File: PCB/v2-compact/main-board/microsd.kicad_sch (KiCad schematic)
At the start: 0 parts

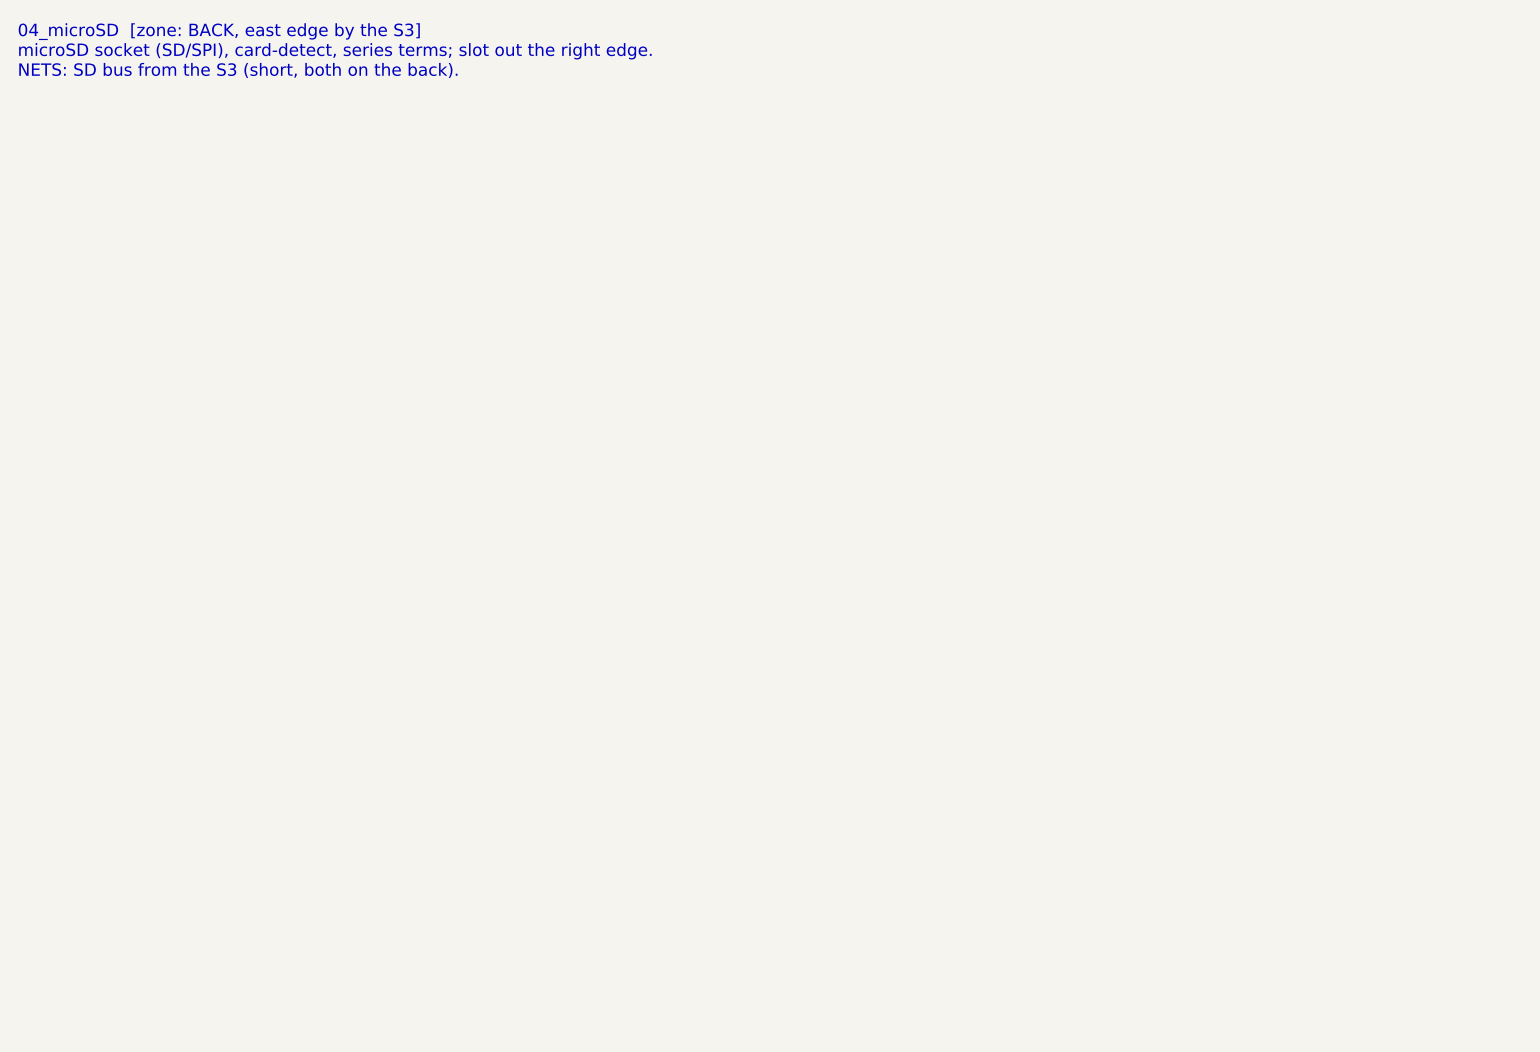
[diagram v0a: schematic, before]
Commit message: Schematics: main board ESP32-S3, microSD, and display/UI sheets
- 02_ESP32-S3: the brain. Shared SPI (LCD_SCK/MOSI + SD_MISO) for TFT and
  microSD, USB data to the USB-C through the ESD, and the full J1 interface to
  the shield (C5 UART + DRDY, I2C to PN532, RV1106 UART, IR, 1-Wire). EN/boot RC
  + decoupling.
- 04_microSD: SPI-mode card with CS pull-up + decoupling.
- 03_Display_UI: SPI TFT header, five nav buttons to GND, two status LEDs.

Netlist-verified: the S3 ties in the other end of every J1 net (isolated labels
on the main board dropped from 12 to 1).
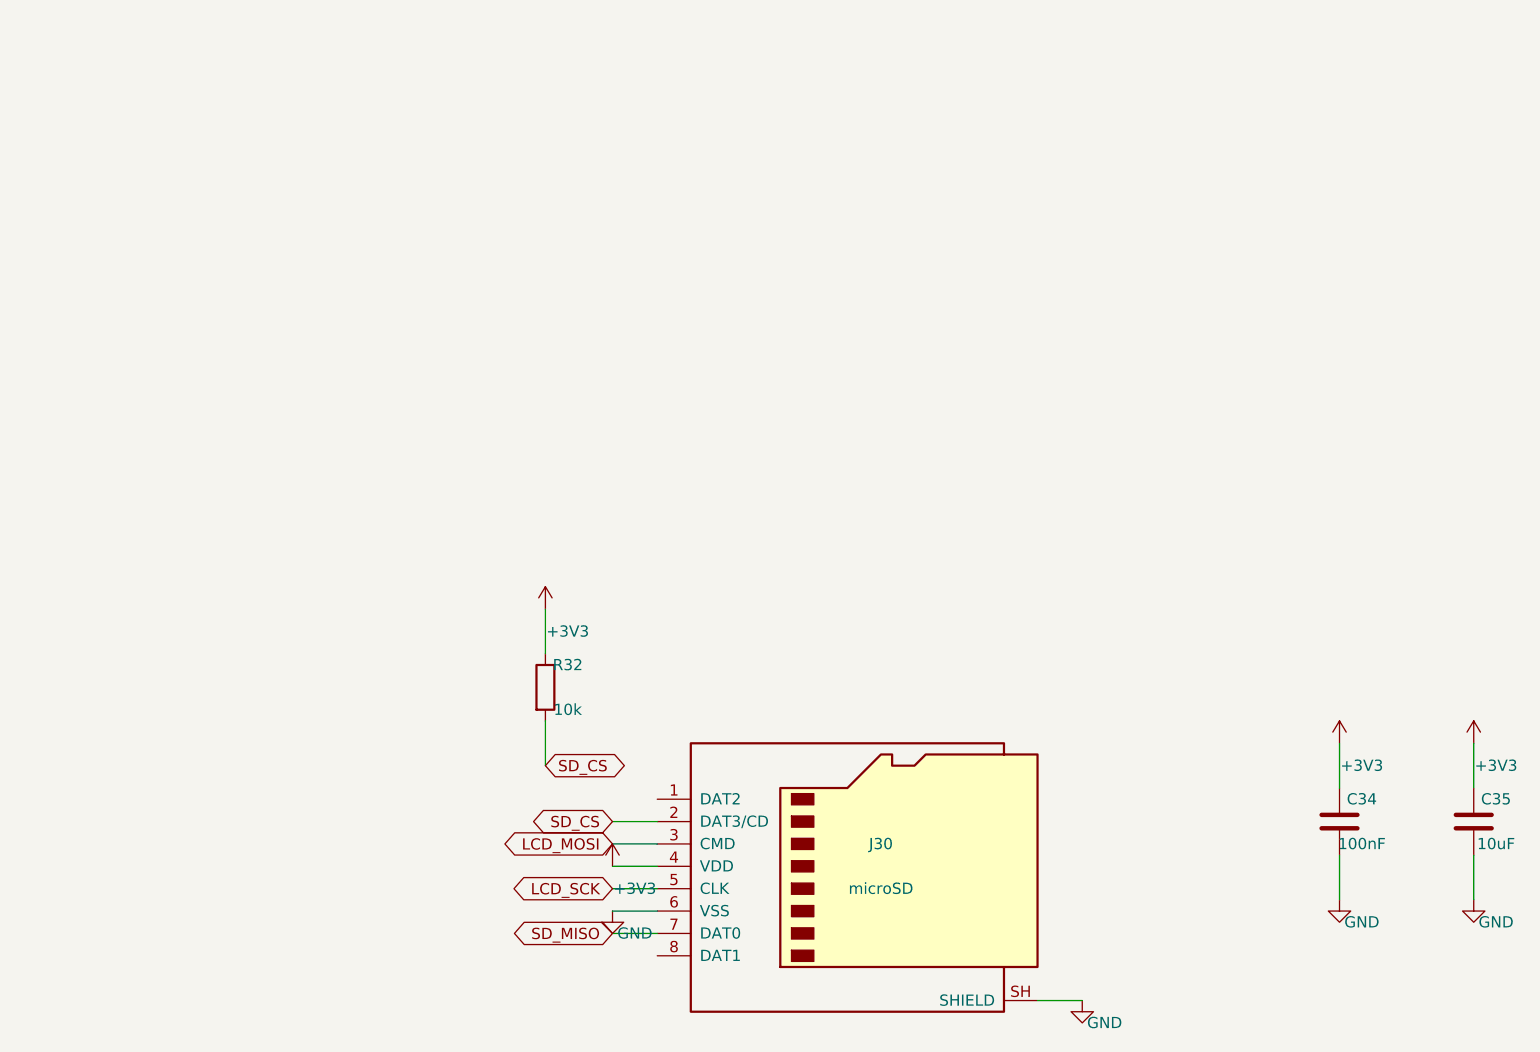
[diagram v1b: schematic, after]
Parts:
- added C34: 100nF, Capacitor_SMD:C_0402_1005Metric, symbol Device:C
- added C35: 10uF, Capacitor_SMD:C_0402_1005Metric, symbol Device:C
- added J30: microSD, Connector_Card:microSD_HC_Hirose_DM3AT-SF-PEJM5, symbol Connector:Micro_SD_Card
- added R32: 10k, Resistor_SMD:R_0402_1005Metric, symbol Device:R
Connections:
- new net +3V3: C34.1, C35.1, J30.4 (VDD), R32.1
- new net GND: C34.2, C35.2, J30.6 (VSS), J30.SH (SHIELD)
- new net LCD_MOSI: J30.3 (CMD)
- new net LCD_SCK: J30.5 (CLK)
- new net SD_CS: J30.2 (DAT3/CD), R32.2
- new net SD_MISO: J30.7 (DAT0)
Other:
- note removed: "04_microSD [zone: BACK, east edge by the S3] microSD socket (SD/SPI), card-detect, series terms; slot out the right edge. NETS: SD bus from the S3 (short, both on the back)."
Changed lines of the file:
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@@
   (paper "A4")
   (title_block (title "04_microSD") (company "YurilLAB"))
-  (text "04_microSD  [zone: BACK, east edge by the S3]
-microSD socket (SD/SPI), card-detect, series terms; slot out the right edge.
-NETS: SD bus from the S3 (short, both on the back)." (at 15 15 0)
-    (effects (font (size 1.4 1.4)) (justify left top)))
+  (symbol (lib_id "Connector:Micro_SD_Card") (at 110.49 110.49 0) (unit 1)
+    (in_bom yes) (on_board yes) (dnp no)
+    (property "Reference" "J30" (at 113.03 107.95 0) (effects (font (size 1.27 1.27))))
+    (property "Value" "microSD" (at 113.03 113.03 0) (effects (font (size 1.27 1.27))))
+    (property "Footprint" "Connector_Card:microSD_HC_Hirose_DM3AT-SF-PEJM5" (at 110.49 110.49 0) (effects (font (size 1.27 1.27)) hide))
+    (pin "1")
+    (pin "2")
+    (pin "3")
+    (pin "4")
+    (pin "5")
+    (pin "6")
+    (pin "7")
+    (pin "8")
+    (pin "SH")
+    (instances (project "SnowOwl-Main" (path "/a1b2c3d4-0001-4001-8001-000000000014" (reference "J30") (unit 1))))
+  )
+  (wire (pts (xy 87.63 105.41) (xy 82.55 105.41)) (stroke (width 0) (type default)))
+  (global_label "SD_CS" (shape bidirectional) (at 82.55 105.41 180) (fields_autoplaced)
+    (effects (font (size 1.27 1.27)) (justify right)))
+  (wire (pts (xy 87.63 107.95) (xy 82.55 107.95)) (stroke (width 0) (type default)))
+  (global_label "LCD_MOSI" (shape bidirectional) (at 82.55 107.95 180) (fields_autoplaced)
+    (effects (font (size 1.27 1.27)) (justify right)))
+  (wire (pts (xy 87.63 110.49) (xy 82.55 110.49)) (stroke (width 0) (type default)))
+  (symbol (lib_id "power:+3V3") (at 82.55 110.49 0) (unit 1)
+    (in_bom yes) (on_board yes) (dnp no)
+    (property "Reference" "#PWR0774B37" (at 85.09 107.95 0) (effects (font (size 1.27 1.27)) hide))
+    (property "Value" "+3V3" (at 85.09 113.03 0) (effects (font (size 1.27 1.27))))
+    (property "Footprint" "" (at 82.55 110.49 0) (effects (font (size 1.27 1.27)) hide))
+    (pin "1")
+    (instances (project "SnowOwl-Main" (path "/a1b2c3d4-0001-4001-8001-000000000014" (reference "#PWR0774B37") (unit 1))))
+  )
+  (wire (pts (xy 87.63 113.03) (xy 82.55 113.03)) (stroke (width 0) (type default)))
+  (global_label "LCD_SCK" (shape bidirectional) (at 82.55 113.03 180) (fields_autoplaced)
+    (effects (font (size 1.27 1.27)) (justify right)))
+  (wire (pts (xy 87.63 115.57) (xy 82.55 115.57)) (stroke (width 0) (type default)))
+  (symbol (lib_id "power:GND") (at 82.55 115.57 0) (unit 1)
+    (in_bom yes) (on_board yes) (dnp no)
+    (property "Reference" "#PWR94C76D4" (at 85.09 113.03 0) (effects (font (size 1.27 1.27)) hide))
+    (property "Value" "GND" (at 85.09 118.11 0) (effects (font (size 1.27 1.27))))
+    (property "Footprint" "" (at 82.55 115.57 0) (effects (font (size 1.27 1.27)) hide))
+    (pin "1")
+    (instances (project "SnowOwl-Main" (path "/a1b2c3d4-0001-4001-8001-000000000014" (reference "#PWR94C76D4") (unit 1))))
+  )
+  (wire (pts (xy 87.63 118.11) (xy 82.55 118.11)) (stroke (width 0) (type default)))
+  (global_label "SD_MISO" (shape bidirectional) (at 82.55 118.11 180) (fields_autoplaced)
+    (effects (font (size 1.27 1.27)) (justify right)))
+  (wire (pts (xy 130.81 125.73) (xy 135.89 125.73)) (stroke (width 0) (type default)))
+  (symbol (lib_id "power:GND") (at 135.89 125.73 0) (unit 1)
+    (in_bom yes) (on_board yes) (dnp no)
+    (property "Reference" "#PWR2EDC1B4" (at 138.43 123.19 0) (effects (font (size 1.27 1.27)) hide))
+    (property "Value" "GND" (at 138.43 128.27 0) (effects (font (size 1.27 1.27))))
+    (property "Footprint" "" (at 135.89 125.73 0) (effects (font (size 1.27 1.27)) hide))
+    (pin "1")
+    (instances (project "SnowOwl-Main" (path "/a1b2c3d4-0001-4001-8001-000000000014" (reference "#PWR2EDC1B4") (unit 1))))
+  )
+  (symbol (lib_id "Device:C") (at 165.1 105.41 0) (unit 1)
+    (in_bom yes) (on_board yes) (dnp no)
+    (property "Reference" "C34" (at 167.64 102.87 0) (effects (font (size 1.27 1.27))))
+    (property "Value" "100nF" (at 167.64 107.95 0) (effects (font (size 1.27 1.27))))
+    (property "Footprint" "Capacitor_SMD:C_0402_1005Metric" (at 165.1 105.41 0) (effects (font (size 1.27 1.27)) hide))
+    (pin "1")
+    (pin "2")
+    (instances (project "SnowOwl-Main" (path "/a1b2c3d4-0001-4001-8001-000000000014" (reference "C34") (unit 1))))
+  )
+  (wire (pts (xy 165.1 101.6) (xy 165.1 96.52)) (stroke (width 0) (type default)))
+  (symbol (lib_id "power:+3V3") (at 165.1 96.52 0) (unit 1)
+    (in_bom yes) (on_board yes) (dnp no)
+    (property "Reference" "#PWR30BBC56" (at 167.64 93.98 0) (effects (font (size 1.27 1.27)) hide))
+    (property "Value" "+3V3" (at 167.64 99.06 0) (effects (font (size 1.27 1.27))))
+    (property "Footprint" "" (at 165.1 96.52 0) (effects (font (size 1.27 1.27)) hide))
+    (pin "1")
+    (instances (project "SnowOwl-Main" (path "/a1b2c3d4-0001-4001-8001-000000000014" (reference "#PWR30BBC56") (unit 1))))
+  )
+  (wire (pts (xy 165.1 109.22) (xy 165.1 114.3)) (stroke (width 0) (type default)))
+  (symbol (lib_id "power:GND") (at 165.1 114.3 0) (unit 1)
+    (in_bom yes) (on_board yes) (dnp no)
+    (property "Reference" "#PWRB871CE9" (at 167.64 111.76 0) (effects (font (size 1.27 1.27)) hide))
+    (property "Value" "GND" (at 167.64 116.84 0) (effects (font (size 1.27 1.27))))
+    (property "Footprint" "" (at 165.1 114.3 0) (effects (font (size 1.27 1.27)) hide))
+    (pin "1")
+    (instances (project "SnowOwl-Main" (path "/a1b2c3d4-0001-4001-8001-000000000014" (reference "#PWRB871CE9") (unit 1))))
+  )
+  (symbol (lib_id "Device:C") (at 180.34 105.41 0) (unit 1)
+    (in_bom yes) (on_board yes) (dnp no)
+    (property "Reference" "C35" (at 182.88 102.87 0) (effects (font (size 1.27 1.27))))
+    (property "Value" "10uF" (at 182.88 107.95 0) (effects (font (size 1.27 1.27))))
+    (property "Footprint" "Capacitor_SMD:C_0402_1005Metric" (at 180.34 105.41 0) (effects (font (size 1.27 1.27)) hide))
+    (pin "1")
+    (pin "2")
+    (instances (project "SnowOwl-Main" (path "/a1b2c3d4-0001-4001-8001-000000000014" (reference "C35") (unit 1))))
+  )
+  (wire (pts (xy 180.34 101.6) (xy 180.34 96.52)) (stroke (width 0) (type default)))
+  (symbol (lib_id "power:+3V3") (at 180.34 96.52 0) (unit 1)
+    (in_bom yes) (on_board yes) (dnp no)
+    (property "Reference" "#PWR4B0D688" (at 182.88 93.98 0) (effects (font (size 1.27 1.27)) hide))
+    (property "Value" "+3V3" (at 182.88 99.06 0) (effects (font (size 1.27 1.27))))
+    (property "Footprint" "" (at 180.34 96.52 0) (effects (font (size 1.27 1.27)) hide))
+    (pin "1")
+    (instances (project "SnowOwl-Main" (path "/a1b2c3d4-0001-4001-8001-000000000014" (reference "#PWR4B0D688") (unit 1))))
+  )
+  (wire (pts (xy 180.34 109.22) (xy 180.34 114.3)) (stroke (width 0) (type default)))
+  (symbol (lib_id "power:GND") (at 180.34 114.3 0) (unit 1)
+    (in_bom yes) (on_board yes) (dnp no)
+    (property "Reference" "#PWRA11DFB9" (at 182.88 111.76 0) (effects (font (size 1.27 1.27)) hide))
+    (property "Value" "GND" (at 182.88 116.84 0) (effects (font (size 1.27 1.27))))
+    (property "Footprint" "" (at 180.34 114.3 0) (effects (font (size 1.27 1.27)) hide))
+    (pin "1")
+    (instances (project "SnowOwl-Main" (path "/a1b2c3d4-0001-4001-8001-000000000014" (reference "#PWRA11DFB9") (unit 1))))
+  )
+  (symbol (lib_id "Device:R") (at 74.93 90.17 0) (unit 1)
+    (in_bom yes) (on_board yes) (dnp no)
+    (property "Reference" "R32" (at 77.47 87.63 0) (effects (font (size 1.27 1.27))))
+    (property "Value" "10k" (at 77.47 92.71 0) (effects (font (size 1.27 1.27))))
+    (property "Footprint" "Resistor_SMD:R_0402_1005Metric" (at 74.93 90.17 0) (effects (font (size 1.27 1.27)) hide))
+    (pin "1")
+    (pin "2")
+    (instances (project "SnowOwl-Main" (path "/a1b2c3d4-0001-4001-8001-000000000014" (reference "R32") (unit 1))))
+  )
+  (wire (pts (xy 74.93 86.36) (xy 74.93 81.28)) (stroke (width 0) (type default)))
+  (symbol (lib_id "power:+3V3") (at 74.93 81.28 0) (unit 1)
+    (in_bom yes) (on_board yes) (dnp no)
+    (property "Reference" "#PWRB53F0C5" (at 77.47 78.74 0) (effects (font (size 1.27 1.27)) hide))
+    (property "Value" "+3V3" (at 77.47 83.82 0) (effects (font (size 1.27 1.27))))
+    (property "Footprint" "" (at 74.93 81.28 0) (effects (font (size 1.27 1.27)) hide))
+    (pin "1")
+    (instances (project "SnowOwl-Main" (path "/a1b2c3d4-0001-4001-8001-000000000014" (reference "#PWRB53F0C5") (unit 1))))
+  )
+  (wire (pts (xy 74.93 93.98) (xy 74.93 99.06)) (stroke (width 0) (type default)))
+  (global_label "SD_CS" (shape bidirectional) (at 74.93 99.06 0) (fields_autoplaced)
+    (effects (font (size 1.27 1.27)) (justify left)))
   (sheet_instances (path "/" (page "1")))
 )
